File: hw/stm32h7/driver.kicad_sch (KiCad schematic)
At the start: 21 parts, among them J3 2-1445100-3, J4 Encoder, U3 DRV8316C

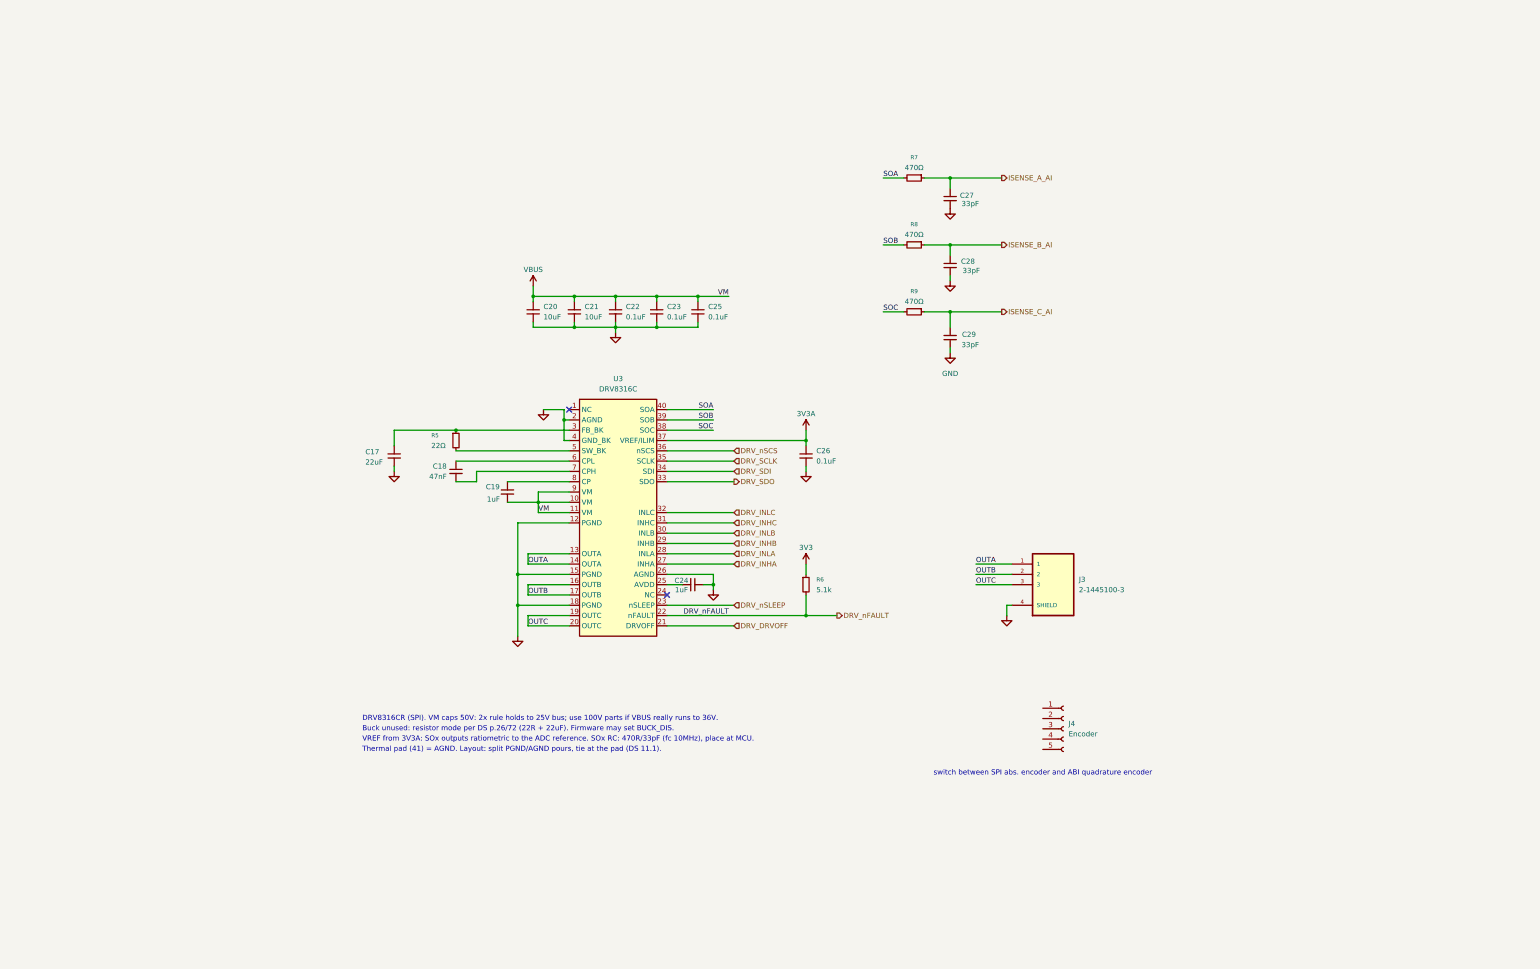
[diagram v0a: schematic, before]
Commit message: WIP: H7 dual-axis encoder ports, VSENSE, LED swap, TPS2553/ESD on J4
- driver sheet: respaced; DRV8316C 3x-PWM pinout; J4 encoder port with
  100R series, 2.2k/5.1k pull-ups, TPD4E05U06 ESD array, TPS2553 current
  limited 5V switch (ENC_EN/ENC_SW_nFLT); phase VSENSE dividers
  (100k/8.2k, 8.2p/100p compensated); R55/R58/R62 footprint -> R_0201
- root sheet: second driver instance (driver2) for the dual-axis plan
- micro sheet: D1/D2 -> WS2812B-2020-V6 (3.3V logic), 5V0 feed
- power sheet: drop 3V3_VSENSE_AI (VREFINT instead), LMR50410 cleanup
- stm32h7.ioc: TIM1/TIM8 PWM, SPI2/SPI3/SPI4, TIM4 encoder, FDCAN1/2,
  QUADSPI bank 2
- datasheets: WS2812B-2020-V6, SK6805-EC15, TPS2553
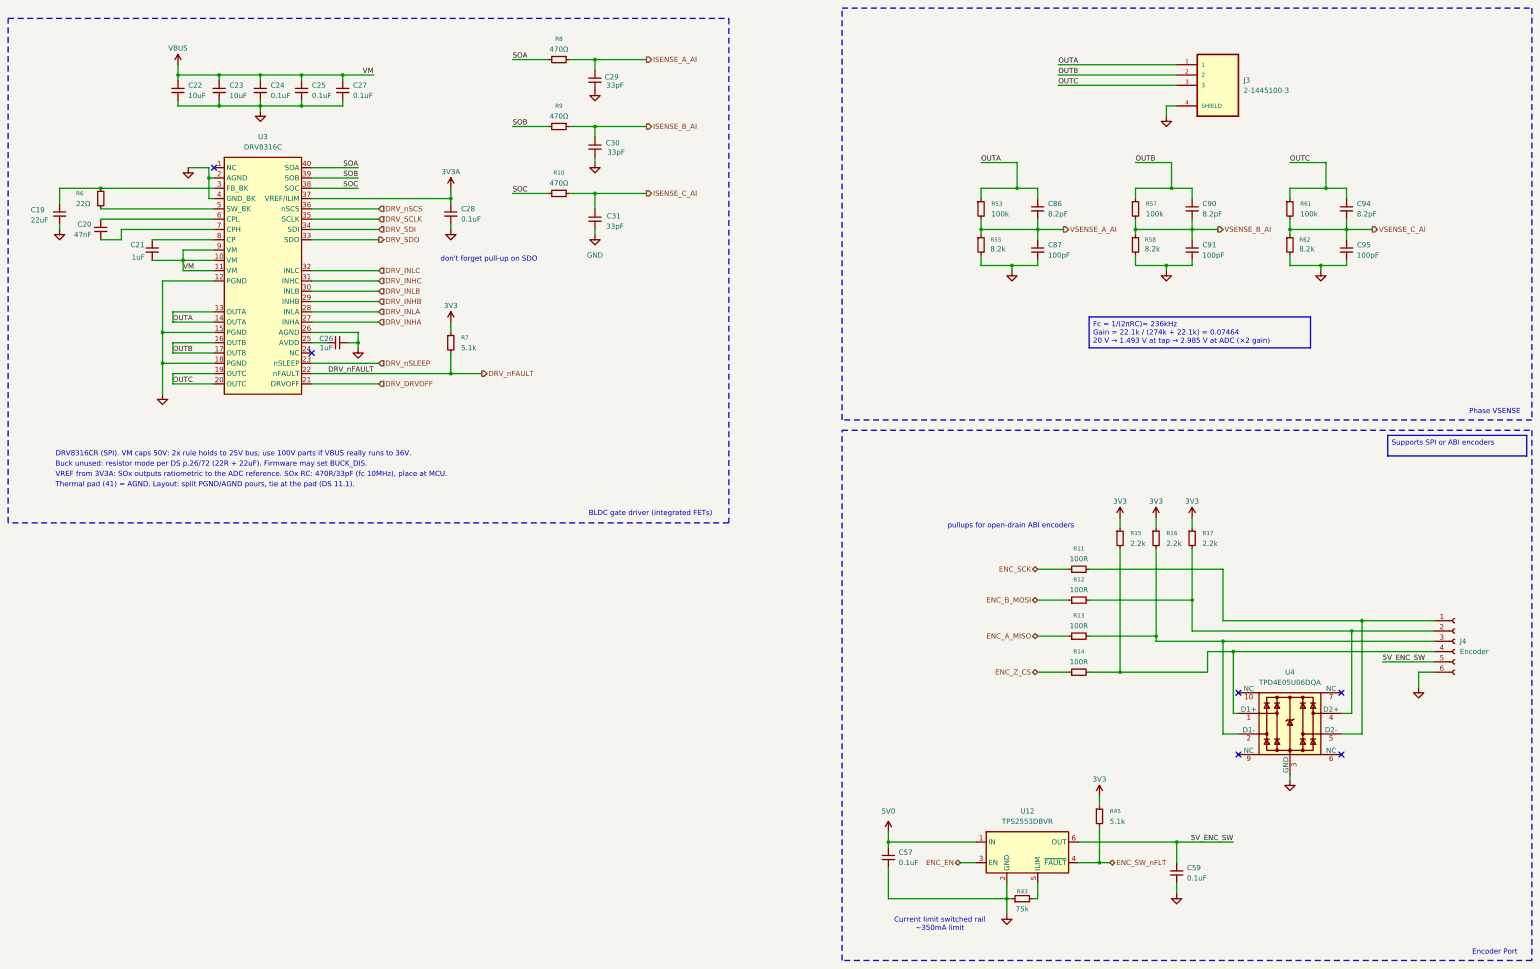
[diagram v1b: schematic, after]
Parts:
- removed J4: Encoder, Connector_Molex:Molex_PicoBlade_53261-0571_1x05-1MP_P1.25mm_Horizontal, symbol Connector:Conn_01x05_Socket
- added C57, C59: 0.1uF, Capacitor_SMD:C_0201_0603Metric, symbol Device:C_Small
- added C86, C90, C94: 8.2pF, Capacitor_SMD:C_0201_0603Metric, symbol Device:C_Small
- added C87, C91, C95: 100pF, Capacitor_SMD:C_0201_0603Metric, symbol Device:C_Small
- added J4: Encoder, Connector_Molex:Molex_PicoBlade_53261-0671_1x06-1MP_P1.25mm_Horizontal, symbol Connector:Conn_01x06_Socket
- added R11, R12, R13, R14: 100R, Resistor_SMD:R_0201_0603Metric, symbol Device:R_Small
- added R15, R16, R17: 2.2k, Resistor_SMD:R_0201_0603Metric, symbol Device:R_Small
- added R43: 75k, Resistor_SMD:R_0201_0603Metric, symbol Device:R_Small
- added R45: 5.1k, Resistor_SMD:R_0201_0603Metric, symbol Device:R_Small
- added R53, R57, R61: 100k, Resistor_SMD:R_0402_1005Metric, symbol Device:R_Small
- added R55, R58, R62: 8.2k, Resistor_SMD:R_0201_0603Metric, symbol Device:R_Small
- added U12: TPS2553DBVR, pcs_lib:SOT-23-6_TI_DBV0006A, symbol pcs_bldc_sym_lib:TPS2553DBVR
- added U4: TPD4E05U06DQA, Package_SON:USON-10_2.5x1.0mm_P0.5mm, symbol Power_Protection:TPD4E05U06DQA
- renumbered C17 to C19, C18 to C20, C19 to C21, C20 to C22, C21 to C23, C22 to C24, C23 to C25, C24 to C26, C25 to C27, C26 to C28, C27 to C29, C28 to C30, C29 to C31, R9 to R10, R5 to R6, R6 to R7, R7 to R8, R8 to R9
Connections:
- net 3V3: now also R15.1, R16.1, R17.1, R45.1
- net GND: now also C57.2, C59.2, C87.2, C91.2, C95.2, J4.6 (Pin_6), R43.1, R55.2, R58.2, R62.2, U12.2 (GND), U4.3 (GND), U4.8 (GND)
- net OUTA: now also C86.1, R53.1
- net OUTB: now also C90.1, R57.1
- net OUTC: now also C94.1, R61.1
- new net: J4.3 (Pin_3), R13.2, R16.2, U4.2 (D1-)
- new net: J4.1 (Pin_1), R11.2, U4.5 (D2-)
- new net: J4.4 (Pin_4), R14.2, R15.2, U4.1 (D1+)
- new net: J4.2 (Pin_2), R12.2, R17.2, U4.4 (D2+)
- new net: R43.2, U12.5 (ILIM)
- new net 5V0: C57.1, U12.1 (IN)
- new net 5V_ENC_SW: C59.1, J4.5 (Pin_5), U12.6 (OUT)
- new net ENC_A_MISO: R13.1
- new net ENC_B_MOSI: R12.1
- new net ENC_EN: U12.3 (EN)
- new net ENC_SCK: R11.1
- new net ENC_SW_nFLT: R45.2, U12.4 (~{FAULT})
- new net ENC_Z_CS: R14.1
- new net VSENSE_A_AI: C86.2, C87.1, R53.2, R55.1
- new net VSENSE_B_AI: C90.2, C91.1, R57.2, R58.1
- new net VSENSE_C_AI: C94.2, C95.1, R61.2, R62.1
- no-connect marks 2 -> 6
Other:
- note added: "BLDC gate driver (integrated FETs)"
- note added: "Current limit switched rail ~350mA limit"
- note added: "Encoder Port"
- note added: "Phase VSENSE"
- note added: "don't forget pull-up on SDO"
- note added: "pullups for open-drain ABI encoders"
- note removed: "switch between SPI abs. encoder and ABI quadrature encoder"
- moved on the sheet: C19, C20, C21, C22, C23, C24, C25, C26, C27, C28, C29, C30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

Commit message: WIP: H7 schematic and PCB layout progress
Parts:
- removed J3: 2-1445100-3, pcs_lib:TE_2-1445100-3, symbol pcs_bldc_sym_lib:2-1445100-3
- removed J4: Encoder, Connector_Molex:Molex_PicoBlade_53261-0671_1x06-1MP_P1.25mm_Horizontal, symbol Connector:Conn_01x06_Socket
- renumbered C19 to C25, C20 to C26, C21 to C27, C22 to C28, C23 to C29, C24 to C30, C25 to C31, C26 to C32, C27 to C33, C28 to C34, C29 to C35, C30 to C36, C31 to C37, C57 to C38, C86 to C39, C87 to C40, C59 to C41, C90 to C42, C91 to C43, C94 to C44, C95 to C45, R7 to R10, R8 to R11, R9 to R12, R10 to R13, R53 to R14, R55 to R15, R43 to R16, R11 to R17, R12 to R18, R13 to R19, R14 to R20, R45 to R21, R15 to R22, R57 to R23, R58 to R24, R16 to R25, R17 to R26, R61 to R27, R62 to R28, R6 to R9, U12 to U4, U4 to U5
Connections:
- net EXT_ENC_A_MISO: now reaches R19.2, R25.2
- net EXT_ENC_A_MISO: now also U5.1 (D1+), U5.10 (NC); no longer U5.2 (D1-)
- net EXT_ENC_SCK: now reaches R17.2
- net EXT_ENC_SCK: now also U5.4 (D2+), U5.7 (NC); no longer U5.5 (D2-)
- net EXT_ENC_Z_CS: now reaches R20.2, R22.2
- net EXT_ENC_Z_CS: now also U5.5 (D2-), U5.6 (NC); no longer U5.1 (D1+)
- net EXT_ENC_B_MOSI: now reaches R18.2, R26.2
- net EXT_ENC_B_MOSI: now also U5.2 (D1-), U5.9 (NC); no longer U5.4 (D2+)
- no-connect marks 6 -> 2
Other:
- moved on the sheet: C39, C40, C42, C43, C44, C45, R14, R15, R23, R24, R27, R28
